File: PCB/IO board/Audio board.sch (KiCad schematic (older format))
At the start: 0 parts

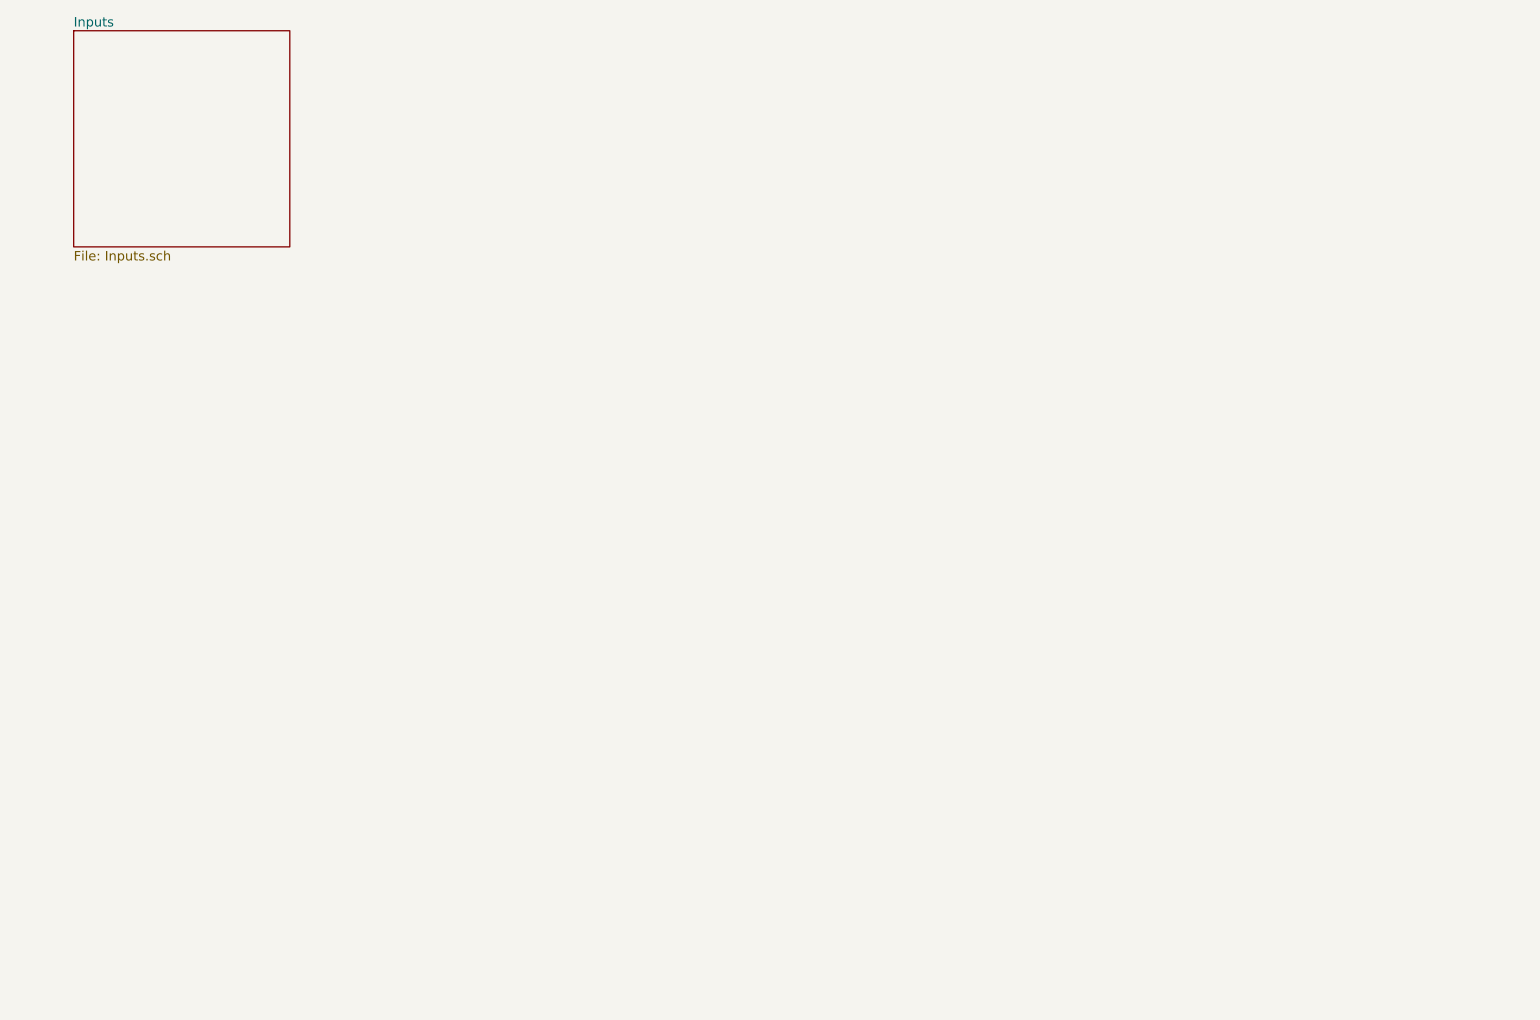
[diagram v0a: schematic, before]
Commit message: Schematics without ESP
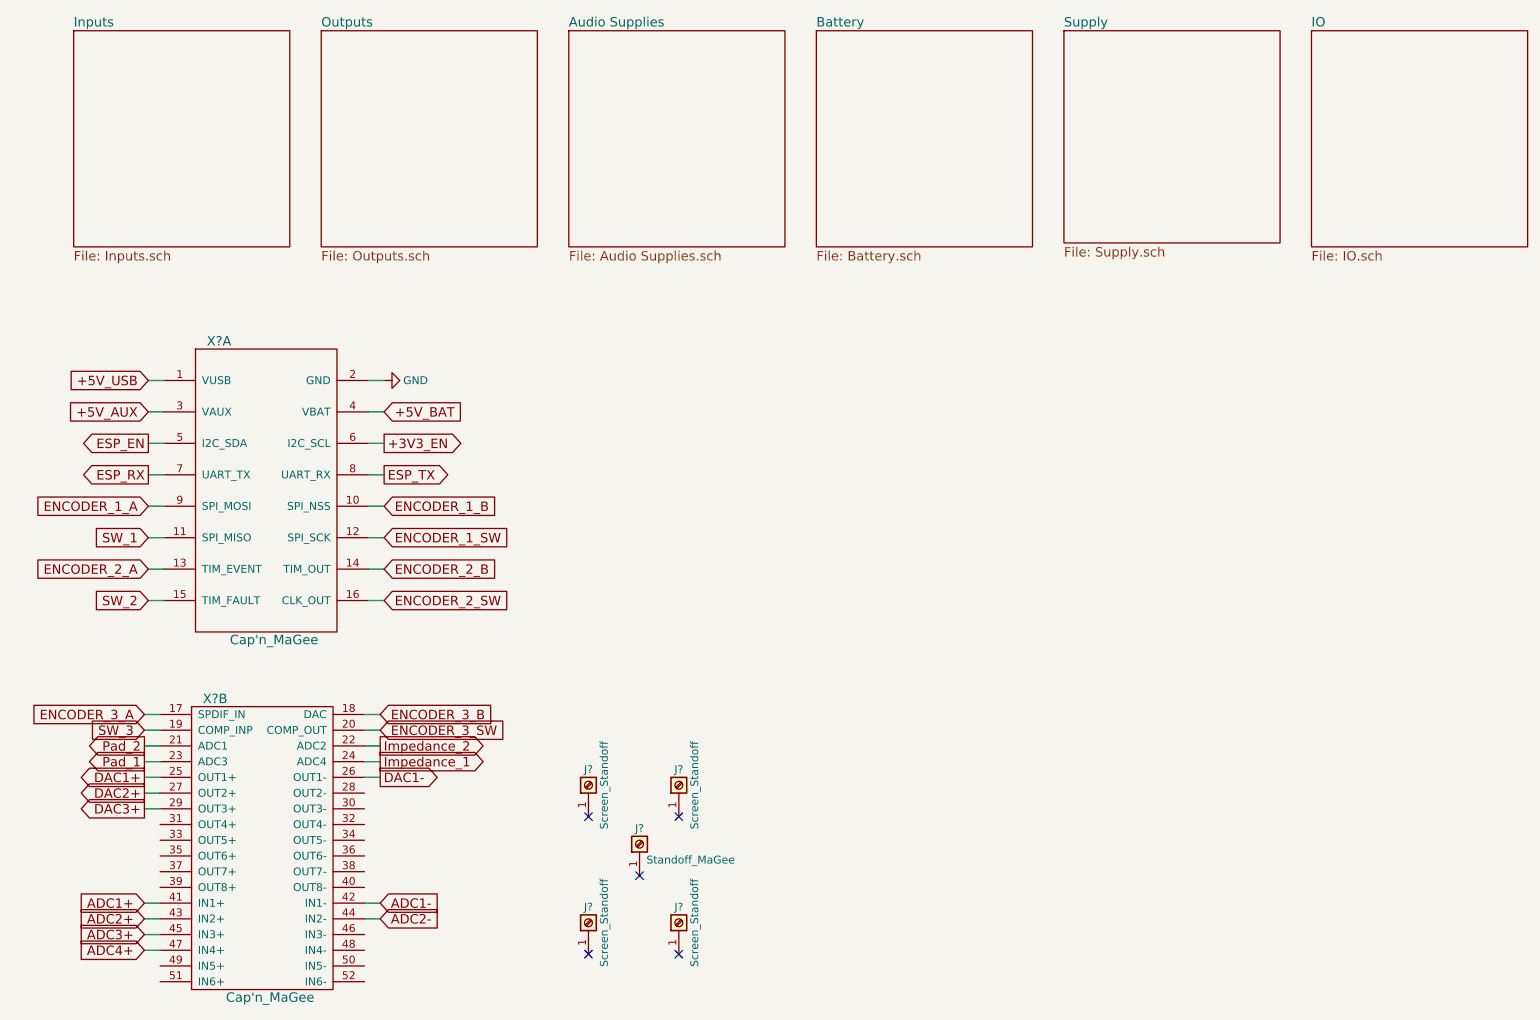
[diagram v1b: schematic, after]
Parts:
- added J?: Standoff_MaGee, symbol Screw_Terminal_01x01
- added J? (x4): Screen_Standoff, symbol Screw_Terminal_01x01
- added X? (x2): Cap'n_MaGee, symbol Cap'n_MaGee
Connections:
- new net +3V3_EN: X?.6 (I2C_SCL)
- new net +5V_AUX: X?.3 (VAUX)
- new net +5V_BAT: X?.4 (VBAT)
- new net +5V_USB: X?.1 (VUSB)
- new net ADC1+: X?.41 (IN1+)
- new net ADC1-: X?.42 (IN1-)
- new net ADC2+: X?.43 (IN2+)
- new net ADC2-: X?.44 (IN2-)
- new net ADC3+: X?.45 (IN3+)
- new net ADC4+: X?.47 (IN4+)
- new net DAC1+: X?.25 (OUT1+)
- new net DAC1-: X?.26 (OUT1-)
- new net DAC2+: X?.27 (OUT2+)
- new net DAC3+: X?.29 (OUT3+)
- new net ENCODER_1_A: X?.9 (SPI_MOSI)
- new net ENCODER_1_B: X?.10 (SPI_NSS)
- new net ENCODER_1_SW: X?.12 (SPI_SCK)
- new net ENCODER_2_A: X?.13 (TIM_EVENT)
- new net ENCODER_2_B: X?.14 (TIM_OUT)
- new net ENCODER_2_SW: X?.16 (CLK_OUT)
- new net ENCODER_3_A: X?.17 (SPDIF_IN)
- new net ENCODER_3_B: X?.18 (DAC)
- new net ENCODER_3_SW: X?.20 (COMP_OUT)
- new net ESP_EN: X?.5 (I2C_SDA)
- new net ESP_RX: X?.7 (UART_TX)
- new net ESP_TX: X?.8 (UART_RX)
- new net GND: X?.2 (GND)
- new net Impedance_1: X?.24 (ADC4)
- new net Impedance_2: X?.22 (ADC2)
- new net Pad_1: X?.23 (ADC3)
- new net Pad_2: X?.21 (ADC1)
- new net SW_1: X?.11 (SPI_MISO)
- new net SW_2: X?.15 (TIM_FAULT)
- new net SW_3: X?.19 (COMP_INP)
- no-connect marks 0 -> 5

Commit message: Schematics Rev 1.0
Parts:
- gave numbers to parts that had none: 6
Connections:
- no-connect marks 5 -> 24
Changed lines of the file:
@@
 $Descr A4 11693 8268
 encoding utf-8
-Sheet 1 7
+Sheet 1 8
 Title ""
 Date ""
@@
 $EndSheet
 $Comp
-L Cap'n_MaGee X?
+L Cap'n_MaGee X101
 U 1 1 5AE2929F
 P 2100 3800
-F 0 "X?" H 1800 4750 60  0000 C CNN
+F 0 "X101" H 1800 4750 60  0000 C CNN
 F 1 "Cap'n_MaGee" H 2150 2850 60  0000 C CNN
 F 2 "" H 1350 3300 60  0001 C CNN
@@
 $EndComp
 $Comp
-L Cap'n_MaGee X?
+L Cap'n_MaGee X101
 U 2 1 5AE292F4
 P 2075 6075
-F 0 "X?" H 1775 7025 60  0000 C CNN
+F 0 "X101" H 1775 7025 60  0000 C CNN
 F 1 "Cap'n_MaGee" H 2125 5125 60  0000 C CNN
 F 2 "" H 1325 5575 60  0001 C CNN
@@
 Text GLabel 2825 5525 2    60   Output ~ 0
 Impedance_1
-Wire Wire Line
-	1325 5425 1425 5425
-Wire Wire Line
-	2725 5525 2825 5525
-Wire Wire Line
-	2725 5425 2825 5425
-Wire Wire Line
-	1325 5525 1425 5525
 Text GLabel 2825 5425 2    60   Output ~ 0
 Impedance_2
@@
 Text GLabel 1350 3700 0    60   Output ~ 0
 ESP_RX
-Wire Wire Line
-	1350 3700 1450 3700
 Text GLabel 2850 3700 2    60   Output ~ 0
 ESP_TX
-Wire Wire Line
-	2750 3700 2850 3700
-Text GLabel 1350 3500 0    60   Output ~ 0
+Text GLabel 1350 3500 0    60   BiDi ~ 0
 ESP_EN
-Wire Wire Line
-	1350 3500 1450 3500
 Text GLabel 2850 3500 2    60   Output ~ 0
 +3V3_EN
-Wire Wire Line
-	2750 3500 2850 3500
 $Sheet
 S 8750 875  1375 1375
@@
 $EndSheet
 $Comp
-L Screw_Terminal_01x01 J?
+L Screw_Terminal_01x01 J103
 U 1 1 5AE3EB9D
 P 4475 6050
-F 0 "J?" V 4575 6050 50  0000 C CNN
+F 0 "J103" V 4575 6050 50  0000 C CNN
 F 1 "Standoff_MaGee" V 4375 5725 50  0000 C CNN
 F 2 "" H 4475 6050 50  0001 C CNN
@@
 Text GLabel 1325 5325 0    60   Input ~ 0
 SW_3
-Wire Wire Line
-	1325 5325 1425 5325
 Text GLabel 2825 5325 2    60   Input ~ 0
 ENCODER_3_SW
-Wire Wire Line
-	2825 5325 2725 5325
 Text GLabel 2825 5225 2    60   Input ~ 0
 ENCODER_3_B
 Text GLabel 1325 5225 0    60   Input ~ 0
 ENCODER_3_A
-Wire Wire Line
-	1325 5225 1425 5225
-Wire Wire Line
-	2725 5225 2825 5225
 Text GLabel 2850 4500 2    60   Input ~ 0
 ENCODER_2_SW
@@
 Text GLabel 1350 4300 0    60   Input ~ 0
 ENCODER_2_A
-Wire Wire Line
-	1350 4300 1450 4300
-Wire Wire Line
-	1350 4500 1450 4500
-Wire Wire Line
-	2750 4300 2850 4300
-Wire Wire Line
-	2750 4500 2850 4500
 Text GLabel 2850 4100 2    60   Input ~ 0
 ENCODER_1_SW
@@
 Text GLabel 1350 3900 0    60   Input ~ 0
 ENCODER_1_A
-Wire Wire Line
-	1350 4100 1450 4100
-Wire Wire Line
-	1350 3900 1450 3900
-Wire Wire Line
-	2750 4100 2850 4100
-Wire Wire Line
-	2750 3900 2850 3900
-$Comp
-L GND #PWR?
+$Comp
+L GND #PWR01
 U 1 1 5AE40091
 P 2850 3100
-F 0 "#PWR?" H 2850 2850 50  0001 C CNN
+F 0 "#PWR01" H 2850 2850 50  0001 C CNN
 F 1 "GND" V 2850 2900 50  0000 C CNN
 F 2 "" H 2850 3100 50  0001 C CNN
@@
 	0    -1   -1   0
 $EndComp
-Wire Wire Line
-	2750 3100 2850 3100
 Text GLabel 2850 3300 2    60   Input ~ 0
 +5V_BAT
-Wire Wire Line
-	2750 3300 2850 3300
 Text GLabel 1350 3300 0    60   Input ~ 0
 +5V_AUX
-Text GLabel 1350 3100 0    60   Input ~ 0
+Text GLabel 1350 3100 0    60   Output ~ 0
 +5V_USB
-Wire Wire Line
-	1350 3100 1450 3100
-Wire Wire Line
-	1350 3300 1450 3300
 Text GLabel 1325 5625 0    60   Output ~ 0
 DAC1+
-Wire Wire Line
-	1325 5625 1425 5625
 Text GLabel 2825 5625 2    60   Output ~ 0
 DAC1-
-Wire Wire Line
-	2725 5625 2825 5625
 Text GLabel 1325 5725 0    60   Output ~ 0
 DAC2+
 Text GLabel 1325 5825 0    60   Output ~ 0
 DAC3+
-Wire Wire Line
-	1325 5725 1425 5725
-Wire Wire Line
-	1325 5825 1425 5825
 Text GLabel 1325 6425 0    60   Input ~ 0
 ADC1+
-Wire Wire Line
-	1325 6425 1425 6425
 Text GLabel 1325 6525 0    60   Input ~ 0
 ADC2+
@@
 Text GLabel 1325 6725 0    60   Input ~ 0
 ADC4+
-Wire Wire Line
-	1325 6525 1425 6525
-Wire Wire Line
-	1325 6625 1425 6625
-Wire Wire Line
-	1325 6725 1425 6725
 Text GLabel 2825 6425 2    60   Input ~ 0
 ADC1-
 Text GLabel 2825 6525 2    60   Input ~ 0
 ADC2-
-Wire Wire Line
-	2725 6425 2825 6425
-Wire Wire Line
-	2725 6525 2825 6525
-$Comp
-L Screw_Terminal_01x01 J?
+$Comp
+L Screw_Terminal_01x01 J101
 U 1 1 5AE41CE9
 P 4150 5675
-F 0 "J?" V 4250 5675 50  0000 C CNN
+F 0 "J101" V 4250 5675 50  0000 C CNN
 F 1 "Screen_Standoff" H 4150 5575 50  0000 C CNN
 F 2 "" H 4150 5675 50  0001 C CNN
@@
 $EndComp
 $Comp
-L Screw_Terminal_01x01 J?
+L Screw_Terminal_01x01 J102
 U 1 1 5AE41DA0
 P 4725 5675
-F 0 "J?" V 4825 5675 50  0000 C CNN
+F 0 "J102" V 4825 5675 50  0000 C CNN
 F 1 "Screen_Standoff" H 4725 5575 50  0000 C CNN
 F 2 "" H 4725 5675 50  0001 C CNN
@@
 $EndComp
 $Comp
-L Screw_Terminal_01x01 J?
+L Screw_Terminal_01x01 J104
 U 1 1 5AE41DCE
 P 4150 6550
-F 0 "J?" V 4250 6550 50  0000 C CNN
+F 0 "J104" V 4250 6550 50  0000 C CNN
 F 1 "Screen_Standoff" H 4150 6450 50  0000 C CNN
 F 2 "" H 4150 6550 50  0001 C CNN
@@
 $EndComp
 $Comp
-L Screw_Terminal_01x01 J?
+L Screw_Terminal_01x01 J105
 U 1 1 5AE41E1C
 P 4725 6550
-F 0 "J?" V 4825 6550 50  0000 C CNN
+F 0 "J105" V 4825 6550 50  0000 C CNN
 F 1 "Screen_Standoff" H 4725 6450 50  0000 C CNN
 F 2 "" H 4725 6550 50  0001 C CNN
@@
 NoConn ~ 4725 6750
 NoConn ~ 4150 6750
+Wire Wire Line
+	2725 6525 2825 6525
+Wire Wire Line
+	2725 6425 2825 6425
+Wire Wire Line
+	1325 6725 1425 6725
+Wire Wire Line
+	1325 6625 1425 6625
+Wire Wire Line
+	1325 6525 1425 6525
+Wire Wire Line
+	1325 6425 1425 6425
+Wire Wire Line
+	1325 5825 1425 5825
+Wire Wire Line
+	1325 5725 1425 5725
+Wire Wire Line
+	2725 5625 2825 5625
+Wire Wire Line
+	1325 5625 1425 5625
+Wire Wire Line
+	1350 3300 1450 3300
+Wire Wire Line
+	1350 3100 1450 3100
+Wire Wire Line
+	2750 3300 2850 3300
+Wire Wire Line
+	2750 3100 2850 3100
+Wire Wire Line
+	2750 3900 2850 3900
+Wire Wire Line
+	2750 4100 2850 4100
+Wire Wire Line
+	1350 3900 1450 3900
+Wire Wire Line
+	1350 4100 1450 4100
+Wire Wire Line
+	2750 4500 2850 4500
+Wire Wire Line
+	2750 4300 2850 4300
+Wire Wire Line
+	1350 4500 1450 4500
+Wire Wire Line
+	1350 4300 1450 4300
+Wire Wire Line
+	2725 5225 2825 5225
+Wire Wire Line
+	1325 5225 1425 5225
+Wire Wire Line
+	2825 5325 2725 5325
+Wire Wire Line
+	1325 5325 1425 5325
+Wire Wire Line
+	2750 3500 2850 3500
+Wire Wire Line
+	1350 3500 1450 3500
+Wire Wire Line
+	2750 3700 2850 3700
+Wire Wire Line
+	1350 3700 1450 3700
+Wire Wire Line
+	1325 5525 1425 5525
+Wire Wire Line
+	2725 5425 2825 5425
+Wire Wire Line
+	2725 5525 2825 5525
+Wire Wire Line
+	1325 5425 1425 5425
+NoConn ~ 1425 5925
+NoConn ~ 1425 6025
+NoConn ~ 1425 6125
+NoConn ~ 1425 6225
+NoConn ~ 1425 6325
+NoConn ~ 2725 5725
+NoConn ~ 2725 5825
+NoConn ~ 2725 5925
+NoConn ~ 2725 6025
+NoConn ~ 2725 6125
+NoConn ~ 2725 6225
+NoConn ~ 2725 6325
+NoConn ~ 2725 6625
+NoConn ~ 2725 6725
+NoConn ~ 2725 6825
+NoConn ~ 2725 6925
+NoConn ~ 1425 6825
+NoConn ~ 1425 6925
+$Sheet
+S 8750 2450 1375 1375
+U 5AE5F321
+F0 "ESP" 60
+F1 "ESP.sch" 60
+$EndSheet
+NoConn ~ 1450 3250
 $EndSCHEMATC

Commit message: Component Placement - No pul-up
ALmost finished component placement expect for pull ups and low pass
filters for switches etc
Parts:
- J101, J102, J104, J105: footprint (none) -> ELECTROMECH:HARWIN_R30-1001002
- J103: footprint (none) -> ELECTROMECH:Keystone_1560A
- X101: footprint (none) -> PCI-e:Mini_PCI-e_Female
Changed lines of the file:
@@
 F 0 "X101" H 1800 4750 60  0000 C CNN
 F 1 "Cap'n_MaGee" H 2150 2850 60  0000 C CNN
-F 2 "" H 1350 3300 60  0001 C CNN
+F 2 "PCI-e:Mini_PCI-e_Female" H 1350 3300 60  0001 C CNN
 F 3 "" H 1350 3300 60  0001 C CNN
 	1    2100 3800
@@
 F 0 "X101" H 1775 7025 60  0000 C CNN
 F 1 "Cap'n_MaGee" H 2125 5125 60  0000 C CNN
-F 2 "" H 1325 5575 60  0001 C CNN
+F 2 "PCI-e:Mini_PCI-e_Female" H 1325 5575 60  0001 C CNN
 F 3 "" H 1325 5575 60  0001 C CNN
 	2    2075 6075
@@
 F 0 "J103" V 4575 6050 50  0000 C CNN
 F 1 "Standoff_MaGee" V 4375 5725 50  0000 C CNN
-F 2 "" H 4475 6050 50  0001 C CNN
+F 2 "ELECTROMECH:Keystone_1560A" H 4475 6050 50  0001 C CNN
 F 3 "" H 4475 6050 50  0001 C CNN
 	1    4475 6050
@@
 F 0 "J101" V 4250 5675 50  0000 C CNN
 F 1 "Screen_Standoff" H 4150 5575 50  0000 C CNN
-F 2 "" H 4150 5675 50  0001 C CNN
+F 2 "ELECTROMECH:HARWIN_R30-1001002" H 4150 5675 50  0001 C CNN
 F 3 "" H 4150 5675 50  0001 C CNN
 	1    4150 5675
@@
 F 0 "J102" V 4825 5675 50  0000 C CNN
 F 1 "Screen_Standoff" H 4725 5575 50  0000 C CNN
-F 2 "" H 4725 5675 50  0001 C CNN
+F 2 "ELECTROMECH:HARWIN_R30-1001002" H 4725 5675 50  0001 C CNN
 F 3 "" H 4725 5675 50  0001 C CNN
 	1    4725 5675
@@
 F 0 "J104" V 4250 6550 50  0000 C CNN
 F 1 "Screen_Standoff" H 4150 6450 50  0000 C CNN
-F 2 "" H 4150 6550 50  0001 C CNN
+F 2 "ELECTROMECH:HARWIN_R30-1001002" H 4150 6550 50  0001 C CNN
 F 3 "" H 4150 6550 50  0001 C CNN
 	1    4150 6550
@@
 F 0 "J105" V 4825 6550 50  0000 C CNN
 F 1 "Screen_Standoff" H 4725 6450 50  0000 C CNN
-F 2 "" H 4725 6550 50  0001 C CNN
+F 2 "ELECTROMECH:HARWIN_R30-1001002" H 4725 6550 50  0001 C CNN
 F 3 "" H 4725 6550 50  0001 C CNN
 	1    4725 6550

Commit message: IO board Rev 1.0 RC-1
Board for inspection by Supervisor
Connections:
- net Impedance_1: now also X101.22 (ADC2); no longer X101.24 (ADC4)
- net Impedance_2: now also X101.24 (ADC4); no longer X101.22 (ADC2)
- net Pad_1: now also X101.21 (ADC1); no longer X101.23 (ADC3)
- net Pad_2: now also X101.23 (ADC3); no longer X101.21 (ADC1)
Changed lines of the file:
@@
 	1    0    0    -1
 $EndComp
+Text GLabel 1325 5425 0    60   Output ~ 0
+Pad_1
+Text GLabel 2825 5425 2    60   Output ~ 0
+Impedance_1
+Text GLabel 2825 5525 2    60   Output ~ 0
+Impedance_2
 Text GLabel 1325 5525 0    60   Output ~ 0
-Pad_1
-Text GLabel 2825 5525 2    60   Output ~ 0
-Impedance_1
-Text GLabel 2825 5425 2    60   Output ~ 0
-Impedance_2
-Text GLabel 1325 5425 0    60   Output ~ 0
 Pad_2
 Text GLabel 1350 3700 0    60   Output ~ 0
